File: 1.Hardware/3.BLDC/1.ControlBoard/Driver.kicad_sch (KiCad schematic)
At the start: 5 parts, among them IC1 FD6288Q, IC2 FD6288Q

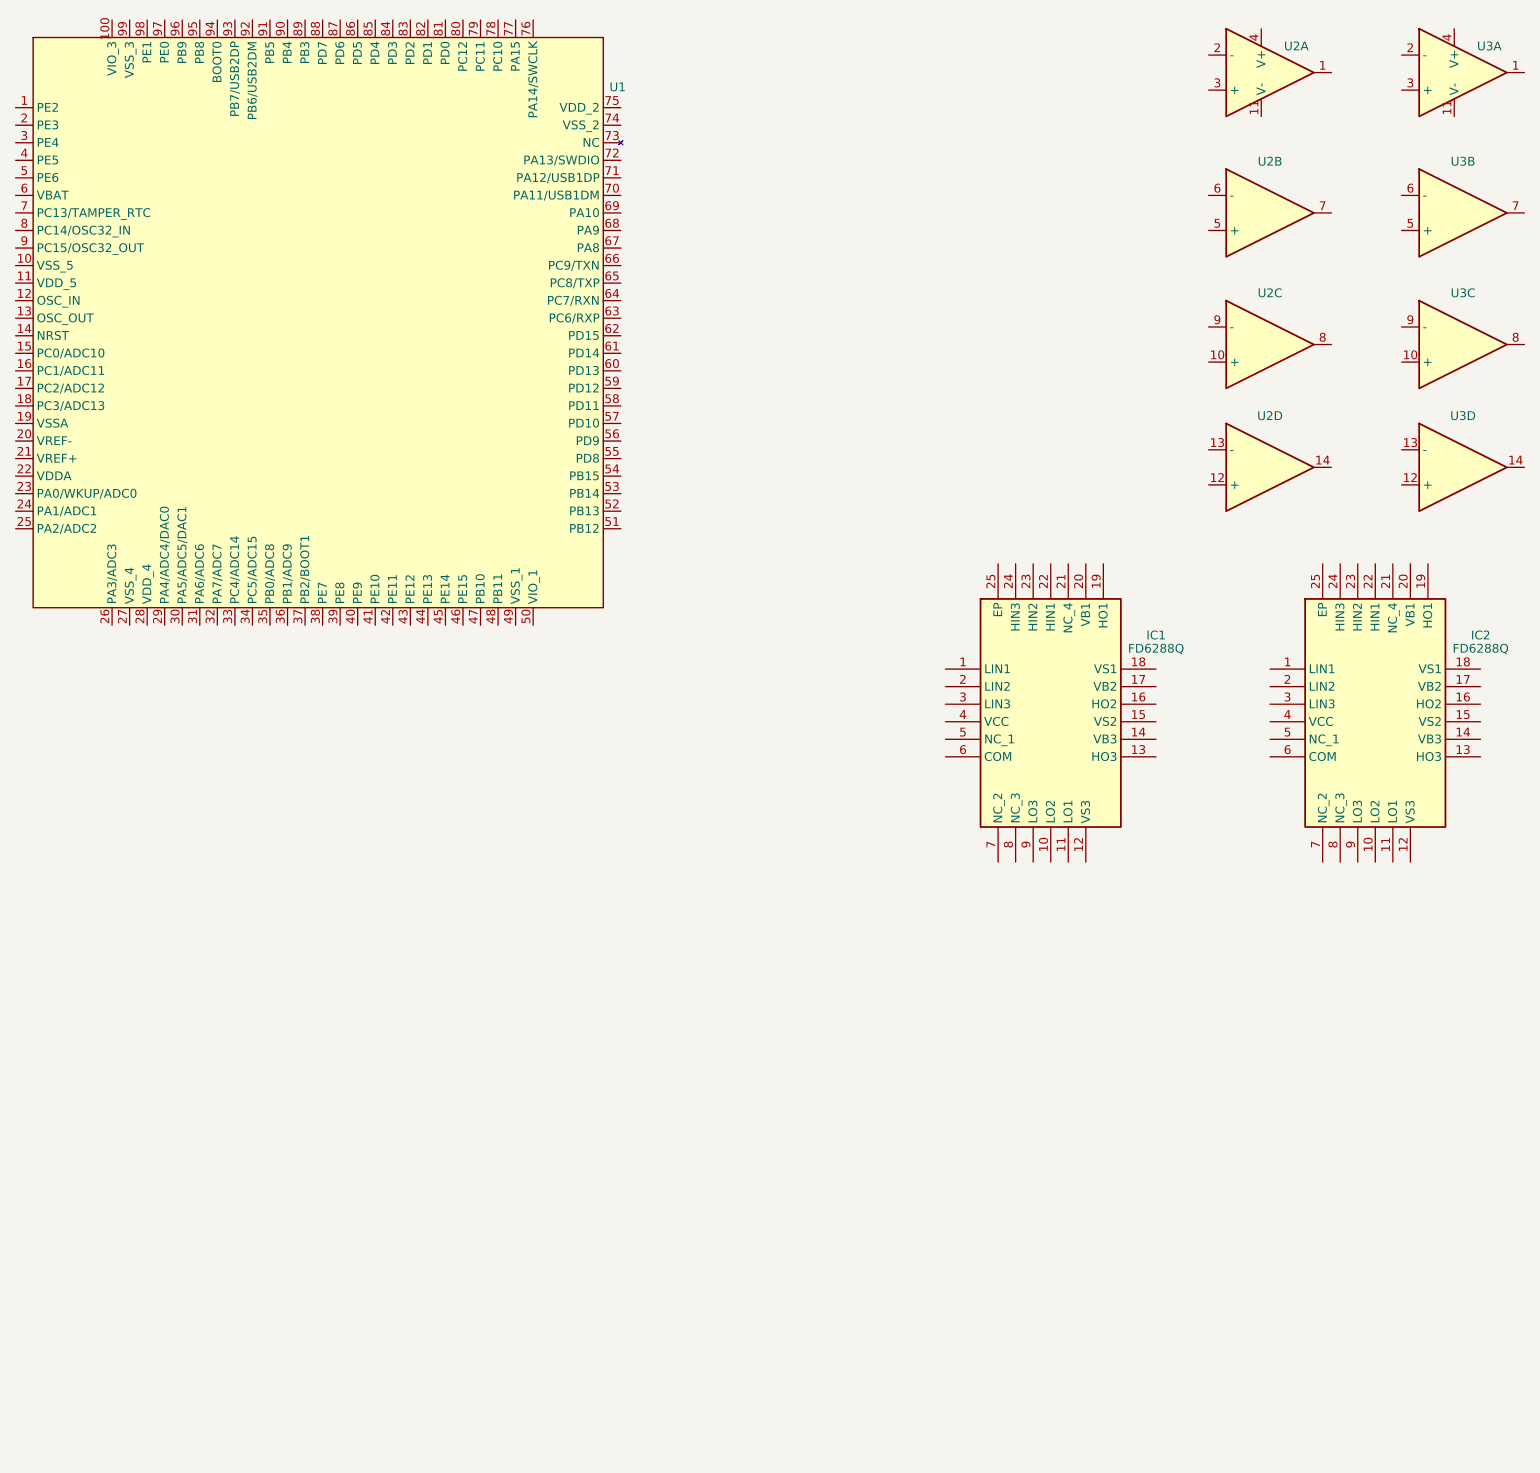
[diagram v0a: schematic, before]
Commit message: Update driver board
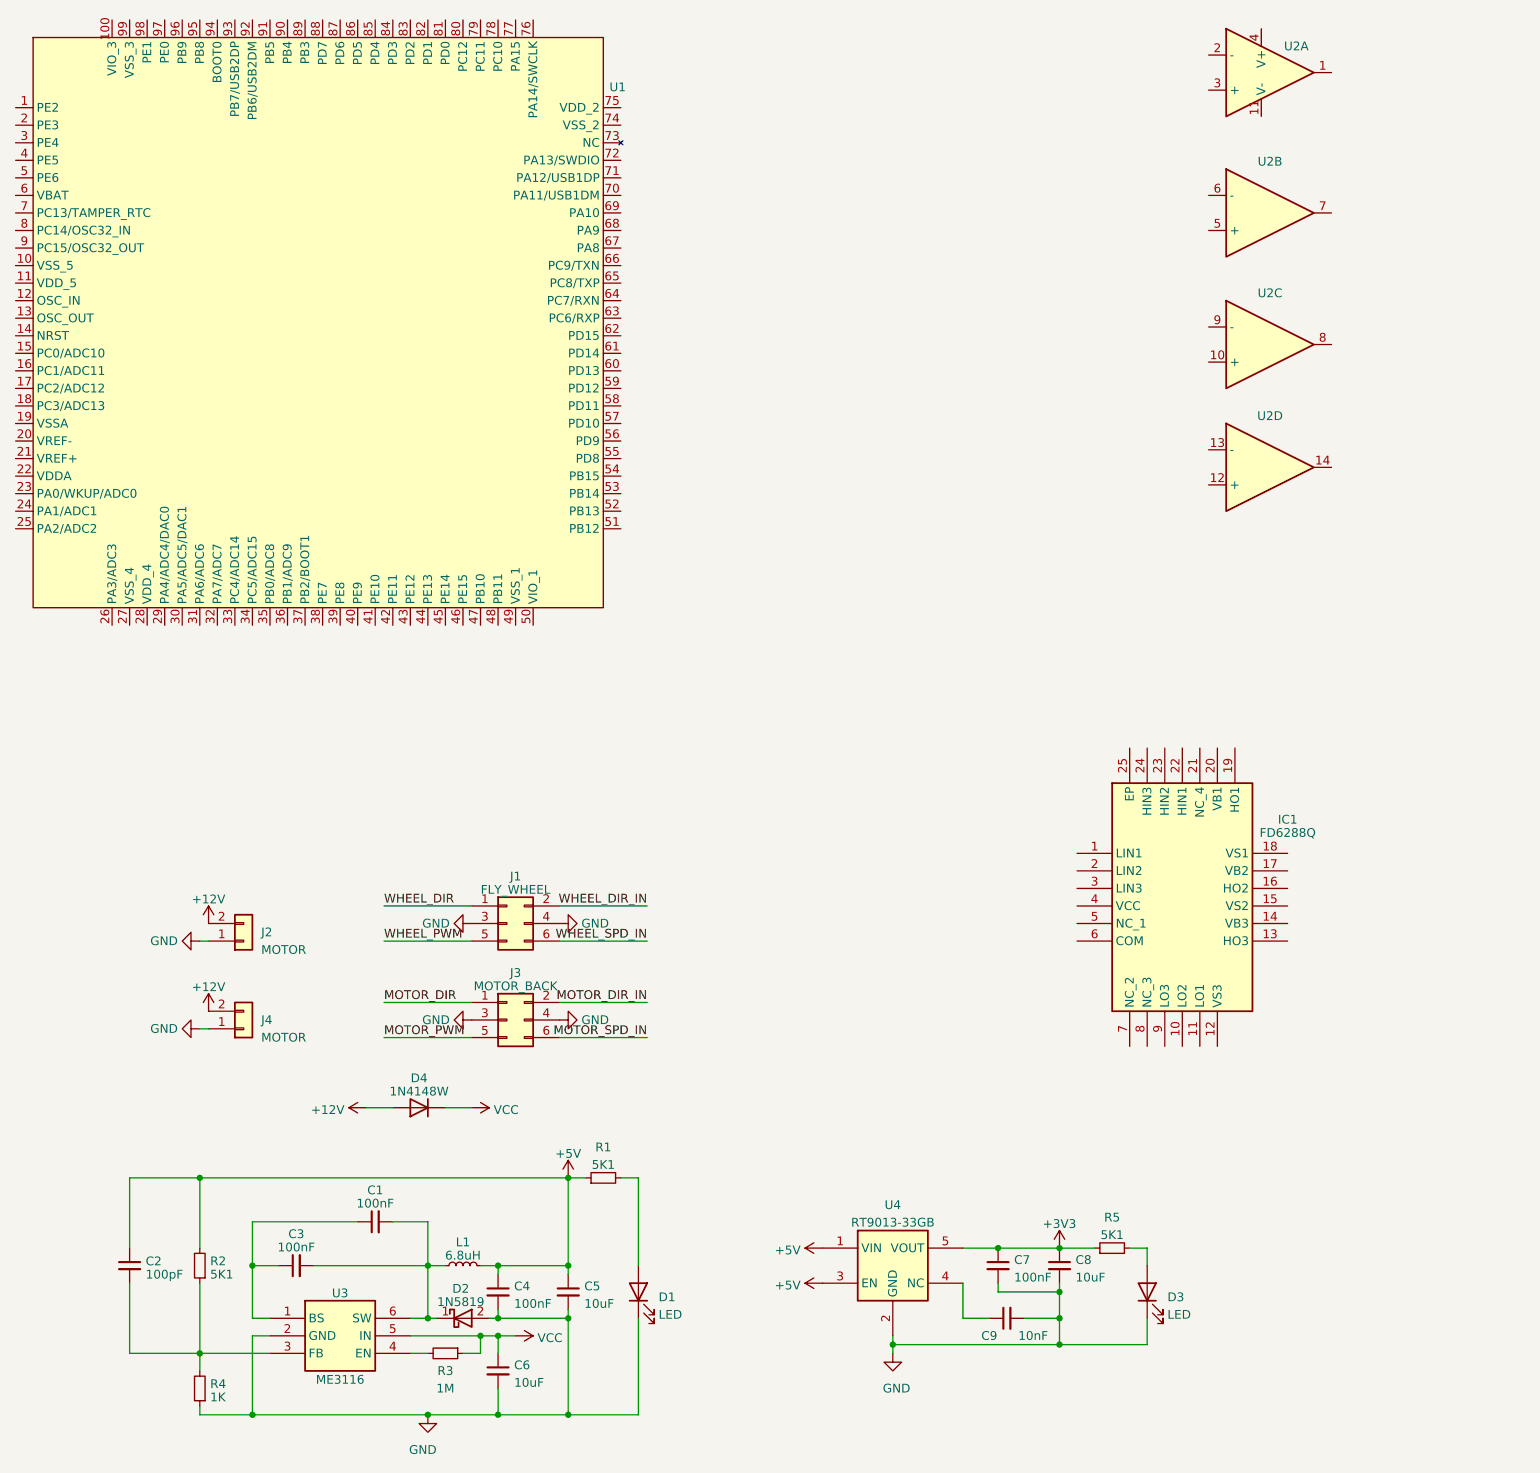
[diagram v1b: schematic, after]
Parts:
- removed IC2: FD6288Q, Package_DFN_QFN:QFN-24-1EP_4x4mm_P0.5mm_EP2.7x2.7mm, symbol ErBW_s:FD6288Q
- removed U3: ~, Package_SO:TSSOP-14_4.4x5mm_P0.65mm, symbol ErBW_s:OPA4377AIPWR
- added C1, C3, C4, C7: 100nF, ErBW_s:C_0402, symbol Device:C_Small
- added C2: 100pF, ErBW_s:C_0402, symbol Device:C_Small
- added C5, C6, C8: 10uF, ErBW_s:C_0402, symbol Device:C_Small
- added C9: 10nF, ErBW_s:C_0402, symbol Device:C_Small
- added D1, D3: LED, LED_SMD:LED_0603_1608Metric, symbol Device:LED
- added D2: 1N5819, ErBW_s:SOD-323, symbol Diode:1N5819WS
- added D4: 1N4148W, Diode_SMD:D_SMA, symbol Diode:1N4148W
- added J1: FLY_WHEEL, Connector_PinSocket_2.54mm:PinSocket_2x03_P2.54mm_Horizontal, symbol Connector_Generic:Conn_02x03_Odd_Even
- added J2, J4: MOTOR, Connector_AMASS:AMASS_XT30PW-M_1x02_P2.50mm_Horizontal, symbol Connector_Generic:Conn_01x02
- added J3: MOTOR_BACK, Connector_PinSocket_2.54mm:PinSocket_2x03_P2.54mm_Horizontal, symbol Connector_Generic:Conn_02x03_Odd_Even
- added L1: 6.8uH, ErBW_s:L_NR201612, symbol Device:L_Small
- added R1, R2, R5: 5K1, ErBW_s:R_0402, symbol Device:R_Small
- added R3: 1M, ErBW_s:R_0402, symbol Device:R_Small
- added R4: 1K, ErBW_s:R_0402, symbol Device:R_Small
- added U3: ME3116, Package_TO_SOT_SMD:SOT-23-6, symbol ErBW_s:ME3116
- added U4: RT9013-33GB, Package_TO_SOT_SMD:SOT-23-5, symbol ErBW_s:RT9013-33GB
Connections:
- new net: C1.2, C3.2, D2.1 (K), L1.1, U3.6 (SW)
- new net: C2.2, R2.1, R4.2, U3.3 (FB)
- new net: D1.2 (A), R1.2
- new net: C1.1, C3.1, U3.1 (BS)
- new net: D3.2 (A), R5.2
- new net: C9.1, U4.4 (NC)
- new net: R3.2, U3.4 (EN)
- new net +12V: D4.2 (A), J2.2 (Pin_2), J4.2 (Pin_2)
- new net +3V3: C7.1, C8.1, R5.1, U4.5 (VOUT)
- new net +5V: C2.1, C4.1, C5.1, L1.2, R1.1, R2.2, U4.1 (VIN), U4.3 (EN)
- new net GND: C4.2, C5.2, C6.2, C7.2, C8.2, C9.2, D1.1 (K), D2.2 (A), D3.1 (K), J1.3 (Pin_3), J1.4 (Pin_4), J2.1 (Pin_1), J3.3 (Pin_3), J3.4 (Pin_4), J4.1 (Pin_1), R4.1, U3.2 (GND), U4.2 (GND)
- new net MOTOR_DIR: J3.1 (Pin_1)
- new net MOTOR_DIR_IN: J3.2 (Pin_2)
- new net MOTOR_PWM: J3.5 (Pin_5)
- new net MOTOR_SPD_IN: J3.6 (Pin_6)
- new net VCC: C6.1, D4.1 (K), R3.1, U3.5 (IN)
- new net WHEEL_DIR: J1.1 (Pin_1)
- new net WHEEL_DIR_IN: J1.2 (Pin_2)
- new net WHEEL_PWM: J1.5 (Pin_5)
- new net WHEEL_SPD_IN: J1.6 (Pin_6)
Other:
- moved on the sheet: IC1

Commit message: Add RT-Thread
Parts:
- added C10, C11, C12, C13, C14: 10uF, ErBW_s:C_0402, symbol Device:C_Small
- added C15, C16, C17: 10nF, ErBW_s:C_0402, symbol Device:C_Small
- added D5, D6, D7: 1N5819, ErBW_s:SOD-323, symbol Diode:1N5819WS
- added J5: Hall, symbol Connector_Generic_MountingPin:Conn_01x06_MountingPin
- added R10, R8, R9: 100R, ErBW_s:R_0402, symbol Device:R_Small
- added R11, R12, R13: 4.7K, ErBW_s:R_0402, symbol Device:R_Small
- added R14, R15, R16, R17, R18, R19, R20, R21, R6: 10K, ErBW_s:R_0402, symbol Device:R_Small
- added R7: 1K, ErBW_s:R_0402, symbol Device:R_Small
- D1, D3: footprint LED_SMD:LED_0603_1608Metric -> ErBW_s:LED_0402
- U1: value ~ -> CH32V307VCT6
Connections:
- net +5V: now also J5.6 (Pin_6), R11.1, R12.1, R13.1
- net GND: now also IC1.25 (EP), IC1.6 (COM), C10.1, C14.2, C15.2, C16.2, C17.2, J5.1 (Pin_1), J5.MP (MountPin), R14.2, R15.1, R16.1, R17.2, R18.1, R19.2, R20.1, R21.2, R7.2
- net MOTOR_DIR: now also R18.2
- net MOTOR_PWM: now also R19.1
- net VCC: now also IC1.4 (VCC), C14.1, D5.2 (A), D6.2 (A), D7.2 (A), R6.1
- net WHEEL_DIR: now also R15.2
- net WHEEL_PWM: now also R14.1
- net PWMAL: now reaches IC1.1 (LIN1)
- net LOB: now reaches IC1.10 (LO2)
- net LOA: now reaches IC1.11 (LO1)
- net at IC1.12 (VS3): now also C13.2
- net HOC: now reaches IC1.13 (HO3)
- net at IC1.14 (VB3): now also C13.1, D7.1 (K)
- net at IC1.15 (VS2): now also C12.2
- net HOB: now reaches IC1.16 (HO2)
- net at IC1.17 (VB2): now also C12.1, D6.1 (K)
- net at IC1.18 (VS1): now also C11.2
- net HOA: now reaches IC1.19 (HO1)
- net PWMBL: now reaches IC1.2 (LIN2)
- net at IC1.20 (VB1): now also C11.1, D5.1 (K)
- net PWMAH: now reaches IC1.22 (HIN1)
- net PWMBH: now reaches IC1.23 (HIN2)
- net PWMCH: now reaches IC1.24 (HIN3)
- net PWMCL: now reaches IC1.3 (LIN3)
- net LOC: now reaches IC1.9 (LO3)
- net MOTOR_DIR_IN renamed MOTOR_DIR_OUT
- net MOTOR_DIR_OUT: now also R20.2
- net MOTOR_SPD_IN renamed MOTOR_SPD_OUT
- net MOTOR_SPD_OUT: now also R21.1
- net WHEEL_DIR_IN renamed WHEEL_DIR_OUT
- net WHEEL_DIR_OUT: now also R16.2
- net WHEEL_SPD_IN renamed WHEEL_SPD_OUT
- net WHEEL_SPD_OUT: now also R17.1
- new net: J5.4 (Pin_4), R10.2
- new net: J5.2 (Pin_2), R8.2
- new net: J5.3 (Pin_3), R9.2
- new net BATTERY: C10.2, R6.2, R7.1
- new net ENC_A: C17.1, R10.1, R11.2
- new net ENC_B: C16.1, R12.2, R9.1
- new net ENC_C: C15.1, R13.2, R8.1
- no-connect marks 0 -> 1
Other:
- moved on the sheet: J1, J3

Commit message: add clion toolchain
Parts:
- added C18: 10uF, ErBW_s:C_0402, symbol Device:C_Small
- added C19, C20, C21, C22: 100nF, ErBW_s:C_0402, symbol Device:C_Small
- added J6: Conn_01x03, symbol Connector_Generic:Conn_01x03
- added R22, R23, R26, R27, R28, R33, R37, R38: 10K, ErBW_s:R_0402, symbol Device:R_Small
- added R24, R25, R29, R30, R31, R32, R34, R35, R36: 1K, ErBW_s:R_0402, symbol Device:R_Small
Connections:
- net +3V3: now also U2.4 (V+), C19.2, R22.2
- net GND: now also U2.11 (V-), C18.2, C19.1, C20.2, C21.2, C22.2, J6.1 (Pin_1), R23.1, R24.2, R29.2, R34.2
- net VCC: now also J6.2 (Pin_2)
- net at U2.10 (+): now also R36.1, R37.1
- net at U2.8: now also R35.2
- net at U2.9 (-): now also R33.2, R34.1
- net at U2.12 (+): now also R22.1, R23.2
- net 1.65V: now reaches U2.13 (-)
- net 1.65V: now also U2.14, C18.1, R26.2, R37.2, R38.2
- net at U2.5 (+): now also R31.1, R38.1
- net at U2.6 (-): now also R28.2, R29.1
- net at U2.7: now also R30.2
- net at U2.1: now also R32.2
- net at U2.2 (-): now also R24.1, R27.2
- net at U2.3 (+): now also R25.1, R26.1
- new net FAN_PWM: J6.3 (Pin_3)
- new net IA: R25.2
- new net IB: R31.2
- new net IC: R36.2
- new net OA: C20.1, R27.1, R32.1
- new net OB: C21.1, R28.1, R30.1
- new net OC: C22.1, R33.1, R35.1
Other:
- moved on the sheet: U2A, U2B, U2C, U2D

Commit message: MotherBoard v1.1 and AIO driver board sch
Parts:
- added C23, C24, C25, C27, C35, C36, C37, C38, C39, C40, C41: 100nF, ErBW_s:C_0402, symbol Device:C_Small
- added C26, C28, C29, C30, C31: 10uF, ErBW_s:C_0402, symbol Device:C_Small
- added C32, C33, C34: 10nF, ErBW_s:C_0402, symbol Device:C_Small
- added C42, C43: 20pF, ErBW_s:C_0402, symbol Device:C_Small
- added D10, D8, D9: 1N5819, ErBW_s:SOD-323, symbol Diode:1N5819WS
- added D11: TVS, Diode_SMD:D_SOD-323, symbol Diode:SD05_SOD323
- added IC2: FD6288Q, Package_DFN_QFN:QFN-24-1EP_4x4mm_P0.5mm_EP2.7x2.7mm, symbol ErBW_s:FD6288Q
- added J10, J9: Conn_02x09_Odd_Even, symbol Connector_Generic:Conn_02x09_Odd_Even
- added J7: Hall, symbol Connector_Generic_MountingPin:Conn_01x06_MountingPin
- added J8: SWD&UART, symbol Connector_Generic_MountingPin:Conn_01x05_MountingPin
- added Q1: S8050, Package_TO_SOT_SMD:SOT-23, symbol Transistor_BJT:2N3055
- added R39, R40, R47, R48, R49, R51, R54, R55, R64, R65, R66: 10K, ErBW_s:R_0402, symbol Device:R_Small
- added R41, R42, R43, R44, R45, R46, R50, R52, R53: 1K, ErBW_s:R_0402, symbol Device:R_Small
- added R56, R57, R58: 100R, ErBW_s:R_0402, symbol Device:R_Small
- added R59, R60, R61: 4.7K, ErBW_s:R_0402, symbol Device:R_Small
- added R62, R63: 0R, ErBW_s:R_0402, symbol Device:R_Small
- added U5: ~, Package_SO:TSSOP-14_4.4x5mm_P0.65mm, symbol ErBW_s:OPA4377AIPWR
- added Y1: 8MHz, ErBW_s:Crystal_SMD_3225_4P, symbol Device:Crystal_GND24_Small
- C10: value 10uF -> 100nF
- J6: value Conn_01x03 -> FAN
- R6: value 10K -> 5K1
- R7: value 1K -> 0R
- U1: value CH32V307VCT6 -> ~
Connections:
- net +3V3 is gone; now on net +3.3V: C19.2, C7.1, C8.1, R22.2, R5.1, U2.4 (V+), U4.5 (VOUT)
- net +5V: now also J7.6 (Pin_6), R59.1, R60.1, R61.1
- net ENC_A: now also U1.91 (PB5)
- net ENC_B: now also U1.90 (PB4)
- net ENC_C: now also U1.89 (PB3)
- net FAN_PWM: now also R6.1, U1.58 (PD11), Q1.1 (B); no longer J6.3 (Pin_3)
- net GND: now also C10.2, R6.2, U1.10 (VSS_5), U1.19 (VSSA), U1.27 (VSS_4), U1.49 (VSS_1), U1.74 (VSS_2), U1.99 (VSS_3), C23.1, C24.2, C25.2, C26.2, C27.2, C30.2, C32.2, C33.2, C34.2, C35.1, C36.1, C37.1, C38.1, C39.1, C40.1, C41.2, C42.2, C43.2, D11.1 (A1), IC2.25 (EP), IC2.6 (COM), J10.11 (Pin_11), J10.13 (Pin_13), J10.14 (Pin_14), J10.15 (Pin_15), J10.16 (Pin_16), J10.17 (Pin_17), J10.9 (Pin_9), J7.1 (Pin_1), J7.MP (MountPin), J8.5 (Pin_5), J8.MP (MountPin), Q1.2 (E), R41.2, R42.2, R50.2, R54.1, R64.1, R65.1, U5.11 (V-), Y1.2, Y1.4; no longer C10.1, J6.1 (Pin_1)
- net HOA: now also J9.1 (Pin_1)
- net HOB: now also J9.3 (Pin_3)
- net HOC: now also J9.2 (Pin_2)
- net IA: now also J9.7 (Pin_7)
- net IB: now also J9.9 (Pin_9)
- net IC: now also J9.8 (Pin_8)
- net LOA: now also IC2.11 (LO1), J9.4 (Pin_4)
- net LOB: now also IC2.10 (LO2), J9.5 (Pin_5)
- net LOC: now also IC2.9 (LO3), J9.6 (Pin_6)
- net MOTOR_DIR: now also U1.64 (PC7/RXN)
- net MOTOR_DIR_OUT: now also U1.60 (PD13)
- net MOTOR_PWM: now also U1.63 (PC6/RXP)
- net MOTOR_SPD_OUT: now also U1.59 (PD12)
- net OA: now also U1.15 (PC0/ADC10)
- net OB: now also U1.16 (PC1/ADC11)
- net OC: now also U1.17 (PC2/ADC12)
- net PWMAH: now also U1.82 (PD1)
- net PWMAL: now also U1.2 (PE3)
- net PWMBH: now also U1.84 (PD3)
- net PWMBL: now also U1.3 (PE4)
- net PWMCH: now also U1.86 (PD5)
- net PWMCL: now also U1.4 (PE5)
- net VCC: now also C30.1, D10.2 (A), D11.2 (A2), D8.2 (A), D9.2 (A), IC2.4 (VCC), J9.11 (Pin_11), J9.12 (Pin_12), J9.13 (Pin_13), J9.14 (Pin_14), J9.15 (Pin_15), J9.16 (Pin_16), J9.17 (Pin_17), J9.18 (Pin_18); no longer R6.1
- net WHEEL_DIR: now also U1.66 (PC9/TXN)
- net WHEEL_DIR_OUT: now also U1.62 (PD15)
- net WHEEL_PWM: now also U1.65 (PC8/TXP)
- net WHEEL_SPD_OUT: now also U1.61 (PD14)
- net +3.3V: now reaches U1.100 (VIO_3)
- net +3.3V: now also U1.11 (VDD_5), U1.28 (VDD_4), U1.50 (VIO_1), U1.6 (VBAT), U1.75 (VDD_2), C23.2, C35.2, C36.2, C37.2, C38.2, C39.2, C40.2, R51.2, R62.2, R66.1, U5.4 (V+)
- net OSC_P: now reaches U1.12 (OSC_IN)
- net OSC_P: now also C43.1, Y1.3
- net OSC_N: now reaches U1.13 (OSC_OUT)
- net OSC_N: now also C42.1, Y1.1
- net RST: now reaches U1.14 (NRST)
- net RST: now also C41.1, R66.2
- net GNDA: now reaches U1.20 (VREF-)
- net GNDA: now also R7.1
- net +3.3VDAC: now reaches U1.21 (VREF+)
- net +3.3VDAC: now also R63.2
- net +3.3VA: now reaches U1.22 (VDDA)
- net +3.3VA: now also C10.1, R62.1, R63.1
- net OU: now reaches U1.33 (PC4/ADC14)
- net OU: now also C24.1, R39.1, R43.1
- net OV: now reaches U1.34 (PC5/ADC15)
- net OV: now also C25.1, R40.1, R44.1
- net OW: now reaches U1.35 (PB0/ADC8)
- net OW: now also C27.1, R49.1, R52.1
- net TEMPERATURE: now reaches U1.36 (PB1/ADC9)
- net TEMPERATURE: now also J9.10 (Pin_10)
- net at U1.37 (PB2/BOOT1): now also R65.2
- net PWMUL: now reaches U1.39 (PE8)
- net PWMUL: now also IC2.1 (LIN1)
- net PWMUH: now reaches U1.40 (PE9)
- net PWMUH: now also IC2.22 (HIN1)
- net PWMVL: now reaches U1.41 (PE10)
- net PWMVL: now also IC2.2 (LIN2)
- net PWMVH: now reaches U1.42 (PE11)
- net PWMVH: now also IC2.23 (HIN2)
- net PWMWL: now reaches U1.43 (PE12)
- net PWMWL: now also IC2.3 (LIN3)
- net PWMWH: now reaches U1.44 (PE13)
- net PWMWH: now also IC2.24 (HIN3)
- net UART3_TX: now reaches U1.47 (PB10)
- net UART3_TX: now also J8.2 (Pin_2)
- net UART3_RX: now reaches U1.48 (PB11)
- net UART3_RX: now also J8.1 (Pin_1)
- net ENC_W: now reaches U1.52 (PB13)
- net ENC_W: now also C34.1, R56.1, R61.2
- net ENC_V: now reaches U1.53 (PB14)
- net ENC_V: now also C33.1, R57.1, R60.2
- net ENC_U: now reaches U1.54 (PB15)
- net ENC_U: now also C32.1, R58.1, R59.2
- net DAP_SWDIO: now reaches U1.72 (PA13/SWDIO)
- net DAP_SWDIO: now also J8.3 (Pin_3)
- net DAP_SWCLK: now reaches U1.76 (PA14/SWCLK)
- net DAP_SWCLK: now also J8.4 (Pin_4)
- net at U1.94 (BOOT0): now also R64.2
- removed net BATTERY: C10.2, R6.2, R7.1
- new net: C29.1, D9.1 (K), IC2.17 (VB2)
- new net: R40.2, R42.1, U5.6 (-)
- new net: R43.2, U5.1
- new net: J7.3 (Pin_3), R57.2
- new net: R39.2, R41.1, U5.2 (-)
- new net: R49.2, R50.1, U5.9 (-)
- new net: R46.1, R48.1, U5.5 (+)
- new net: R44.2, U5.7
- new net: C29.2, IC2.15 (VS2)
- new net: C28.1, D8.1 (K), IC2.20 (VB1)
- new net: C31.2, IC2.12 (VS3)
- new net: C31.1, D10.1 (K), IC2.14 (VB3)
- new net: C28.2, IC2.18 (VS1)
- new net: J7.2 (Pin_2), R56.2
- new net: J7.4 (Pin_4), R58.2
- new net: J6.1 (Pin_1), J6.3 (Pin_3), Q1.3 (C)
- new net: R53.1, R55.1, U5.10 (+)
- new net: R52.2, U5.8
- new net: R45.1, R47.1, U5.3 (+)
- new net: R51.1, R54.2, U5.12 (+)
- new net 1.65v: C26.1, R47.2, R48.2, R55.2, U5.13 (-), U5.14
- new net HOU: IC2.19 (HO1), J10.2 (Pin_2)
- new net HOV: IC2.16 (HO2), J10.4 (Pin_4)
- new net HOW: IC2.13 (HO3), J10.1 (Pin_1)
- new net IU: J10.8 (Pin_8), R45.2
- new net IV: J10.10 (Pin_10), R46.2
- new net IW: J10.7 (Pin_7), R53.2
- new net LOU: J10.3 (Pin_3)
- new net LOV: J10.6 (Pin_6)
- new net LOW: J10.5 (Pin_5)
- no-connect marks 1 -> 42
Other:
- note added: "Copyright (c) 2023, ErBW_s All rights reserved."
- moved on the sheet: C1, C11, C12, C13, C14, C15, C16, C17, C18, C19, C2, C20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
